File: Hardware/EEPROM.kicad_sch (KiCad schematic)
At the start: 3 parts

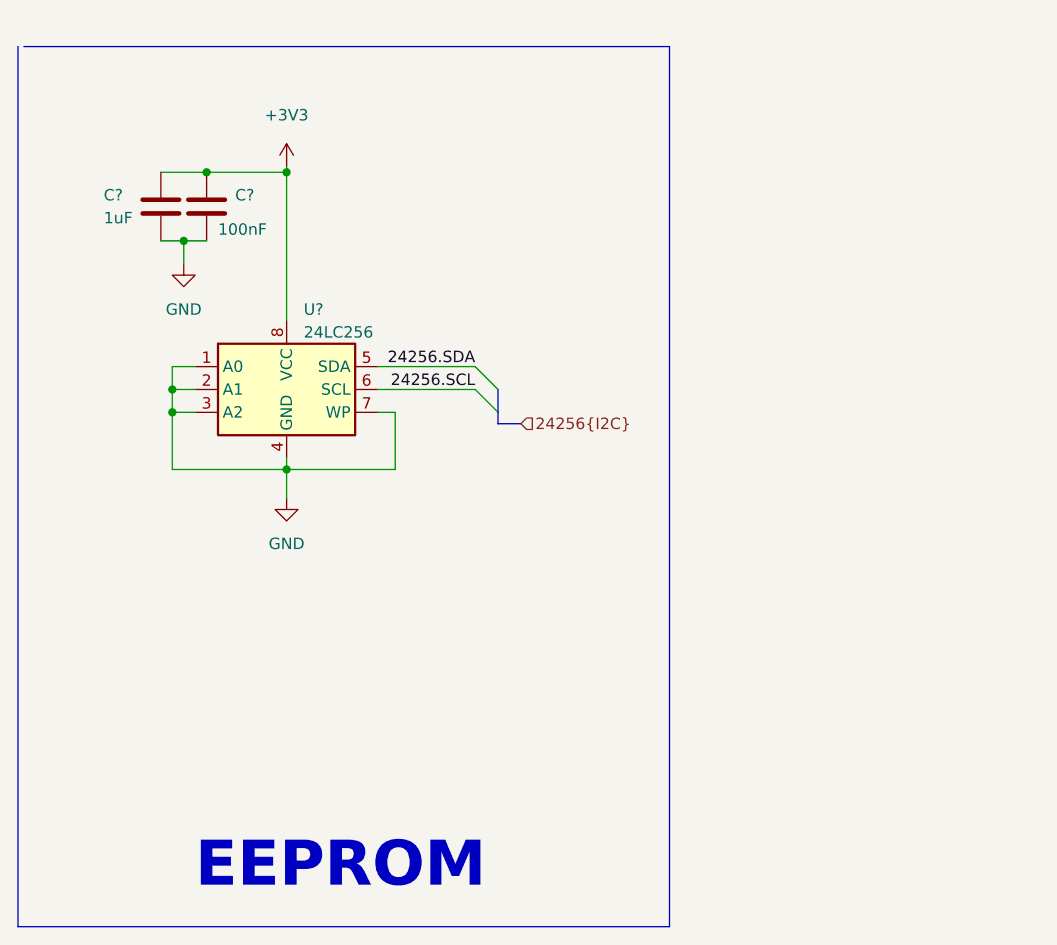
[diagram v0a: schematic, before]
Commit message: nối dây 74hc595(cổng IDC), sửa bus 74HC595
sửa bus 74HC595(SER RCLK SRCLK) theo datasheet kicad
sửa chân các chân 74HC595 trong sch STM và sch 74595
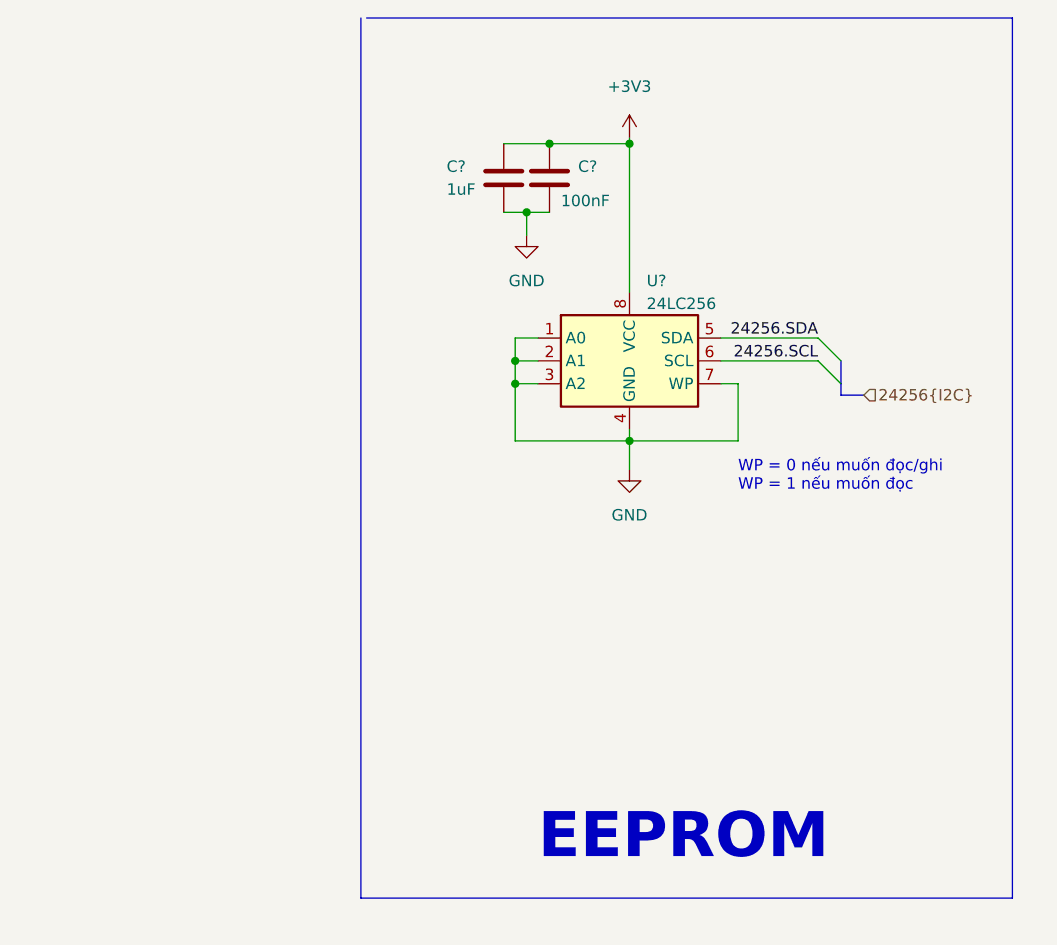
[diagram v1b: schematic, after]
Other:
- note added: "WP = 0 nếu muốn đọc/ghi WP = 1 nếu muốn đọc"
- moved on the sheet: C?, U?

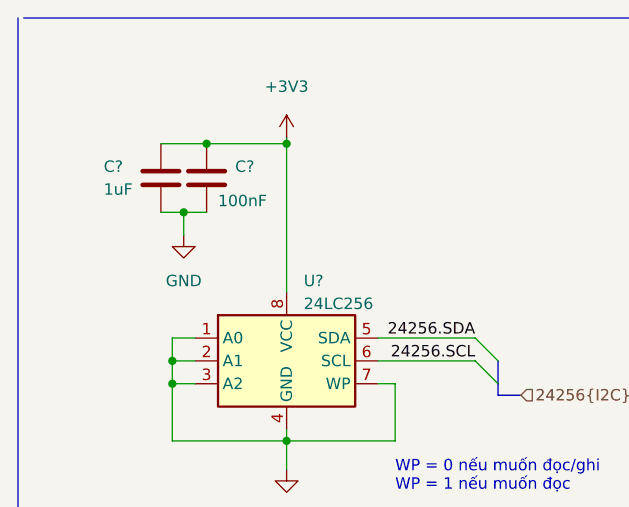
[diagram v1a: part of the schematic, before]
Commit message: add R0603 footprint
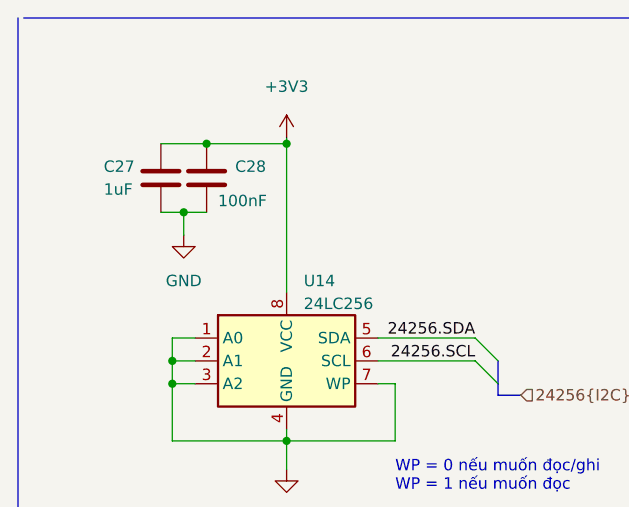
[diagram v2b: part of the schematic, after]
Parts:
- gave numbers to parts that had none: 3
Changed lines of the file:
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@@
   (symbol (lib_id "Device:C") (at 128.905 69.215 0) (unit 1)
     (in_bom yes) (on_board yes)
-    (property "Reference" "C?" (id 0) (at 132.08 67.9449 0)
+    (property "Reference" "C28" (id 0) (at 132.08 67.9449 0)
       (effects (font (size 1.27 1.27)) (justify left))
     )
@@
   (symbol (lib_id "power:GND") (at 137.795 101.6 0) (unit 1)
     (in_bom yes) (on_board yes) (fields_autoplaced)
-    (property "Reference" "#PWR?" (id 0) (at 137.795 107.95 0)
+    (property "Reference" "#PWR0259" (id 0) (at 137.795 107.95 0)
       (effects (font (size 1.27 1.27)) hide)
     )
@@
   (symbol (lib_id "power:GND") (at 126.365 75.565 0) (unit 1)
     (in_bom yes) (on_board yes) (fields_autoplaced)
-    (property "Reference" "#PWR?" (id 0) (at 126.365 81.915 0)
+    (property "Reference" "#PWR0258" (id 0) (at 126.365 81.915 0)
       (effects (font (size 1.27 1.27)) hide)
     )
@@
   (symbol (lib_id "Device:C") (at 123.825 69.215 0) (unit 1)
     (in_bom yes) (on_board yes)
-    (property "Reference" "C?" (id 0) (at 117.475 67.945 0)
+    (property "Reference" "C27" (id 0) (at 117.475 67.945 0)
       (effects (font (size 1.27 1.27)) (justify left))
     )
@@
   (symbol (lib_id "power:+3V3") (at 137.795 64.77 0) (unit 1)
     (in_bom yes) (on_board yes) (fields_autoplaced)
-    (property "Reference" "#PWR?" (id 0) (at 137.795 68.58 0)
+    (property "Reference" "#PWR0257" (id 0) (at 137.795 68.58 0)
       (effects (font (size 1.27 1.27)) hide)
     )
@@
   (symbol (lib_id "Memory_EEPROM:24LC256") (at 137.795 89.535 0) (unit 1)
     (in_bom yes) (on_board yes)
-    (property "Reference" "U?" (id 0) (at 139.7 80.645 0)
+    (property "Reference" "U14" (id 0) (at 139.7 80.645 0)
       (effects (font (size 1.27 1.27)) (justify left))
     )

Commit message: fix MCP41010, fix symbol output header
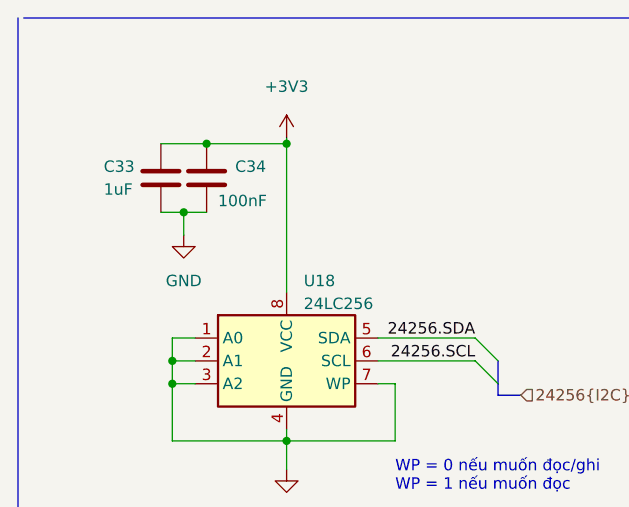
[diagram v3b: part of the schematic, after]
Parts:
- renumbered C27 to C33, C28 to C34, U14 to U18
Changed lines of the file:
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@@
   (symbol (lib_id "Device:C") (at 128.905 69.215 0) (unit 1)
     (in_bom yes) (on_board yes)
-    (property "Reference" "C28" (id 0) (at 132.08 67.9449 0)
+    (property "Reference" "C34" (id 0) (at 132.08 67.9449 0)
       (effects (font (size 1.27 1.27)) (justify left))
     )
@@
   (symbol (lib_id "power:GND") (at 137.795 101.6 0) (unit 1)
     (in_bom yes) (on_board yes) (fields_autoplaced)
-    (property "Reference" "#PWR0259" (id 0) (at 137.795 107.95 0)
+    (property "Reference" "#PWR0160" (id 0) (at 137.795 107.95 0)
       (effects (font (size 1.27 1.27)) hide)
     )
@@
   (symbol (lib_id "power:GND") (at 126.365 75.565 0) (unit 1)
     (in_bom yes) (on_board yes) (fields_autoplaced)
-    (property "Reference" "#PWR0258" (id 0) (at 126.365 81.915 0)
+    (property "Reference" "#PWR0158" (id 0) (at 126.365 81.915 0)
       (effects (font (size 1.27 1.27)) hide)
     )
@@
   (symbol (lib_id "Device:C") (at 123.825 69.215 0) (unit 1)
     (in_bom yes) (on_board yes)
-    (property "Reference" "C27" (id 0) (at 117.475 67.945 0)
+    (property "Reference" "C33" (id 0) (at 117.475 67.945 0)
       (effects (font (size 1.27 1.27)) (justify left))
     )
@@
   (symbol (lib_id "power:+3V3") (at 137.795 64.77 0) (unit 1)
     (in_bom yes) (on_board yes) (fields_autoplaced)
-    (property "Reference" "#PWR0257" (id 0) (at 137.795 68.58 0)
+    (property "Reference" "#PWR0159" (id 0) (at 137.795 68.58 0)
       (effects (font (size 1.27 1.27)) hide)
     )
@@
   (symbol (lib_id "Memory_EEPROM:24LC256") (at 137.795 89.535 0) (unit 1)
     (in_bom yes) (on_board yes)
-    (property "Reference" "U14" (id 0) (at 139.7 80.645 0)
+    (property "Reference" "U18" (id 0) (at 139.7 80.645 0)
       (effects (font (size 1.27 1.27)) (justify left))
     )

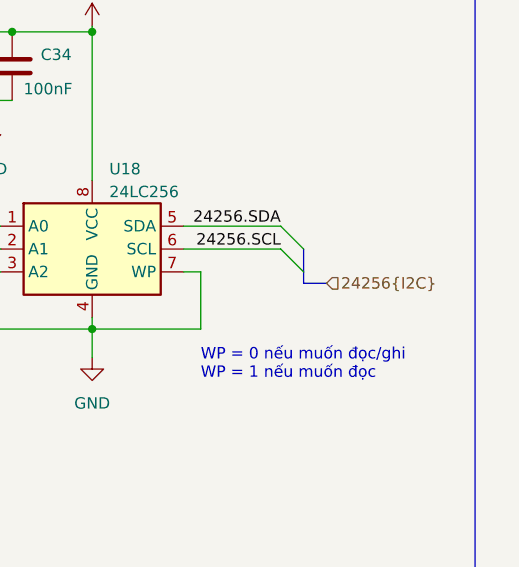
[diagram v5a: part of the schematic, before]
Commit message: add lora, relay, opto, opamp block, led for 74595. Delete RT9193, connect boot0,1 to GND. Fix footprint crystal 8M, 74HC595, IDC pin
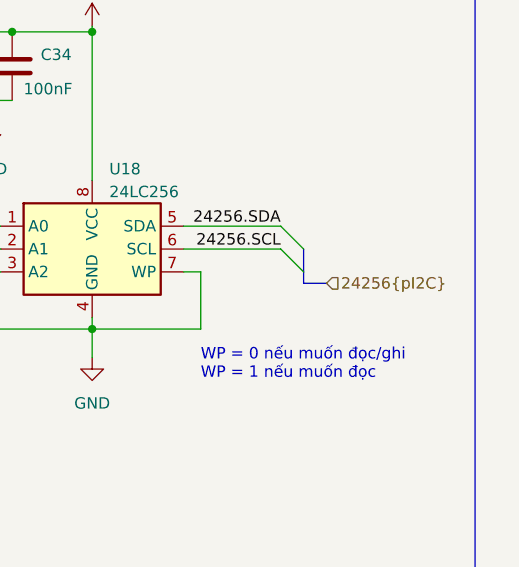
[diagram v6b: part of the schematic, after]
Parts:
- C33, C34: footprint IVS_FOOTPRINTS:C0603 -> IVS_FOOTPRINTS:C_0603
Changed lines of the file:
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@@
     (effects (font (size 1.27 1.27)) (justify right bottom))
   )
-  (hierarchical_label "24256{I2C}" (shape input) (at 163.83 93.345 0) (fields_autoplaced)
+  (hierarchical_label "24256{pI2C}" (shape input) (at 163.83 93.345 0) (fields_autoplaced)
     (effects (font (size 1.27 1.27)) (justify left))
   )
@@
       (effects (font (size 1.27 1.27)) (justify left))
     )
-    (property "Footprint" "IVS_FOOTPRINTS:C0603" (at 129.8702 73.025 0)
+    (property "Footprint" "IVS_FOOTPRINTS:C_0603" (at 129.8702 73.025 0)
       (effects (font (size 1.27 1.27)) hide)
     )
@@
     )
   )
-  (symbol (lib_id "power:GND") (at 137.795 101.6 0) (unit 1)
+  (symbol (lib_name "GND_1") (lib_id "power:GND") (at 137.795 101.6 0) (unit 1)
     (in_bom yes) (on_board yes) (dnp no) (fields_autoplaced)
     (property "Reference" "#PWR0164" (at 137.795 107.95 0)
@@
       (effects (font (size 1.27 1.27)) (justify left))
     )
-    (property "Footprint" "IVS_FOOTPRINTS:C0603" (at 124.7902 73.025 0)
+    (property "Footprint" "IVS_FOOTPRINTS:C_0603" (at 124.7902 73.025 0)
       (effects (font (size 1.27 1.27)) hide)
     )
